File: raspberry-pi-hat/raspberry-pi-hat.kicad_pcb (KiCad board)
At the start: 2 copper layers, 6.6 x 9.1 mm, 28 parts, among them J1 IR_IN_JACK, J2 IR_OUT_JACK, J3 ADC0_JACK, J4 ADC1_JACK, J5 IR_IN_JMP, J6 IR_OUT_JMP, P1 RPi-GPIO, Q1 IRLML2803TRPBF, U1 MCP3204, U2 74AC86

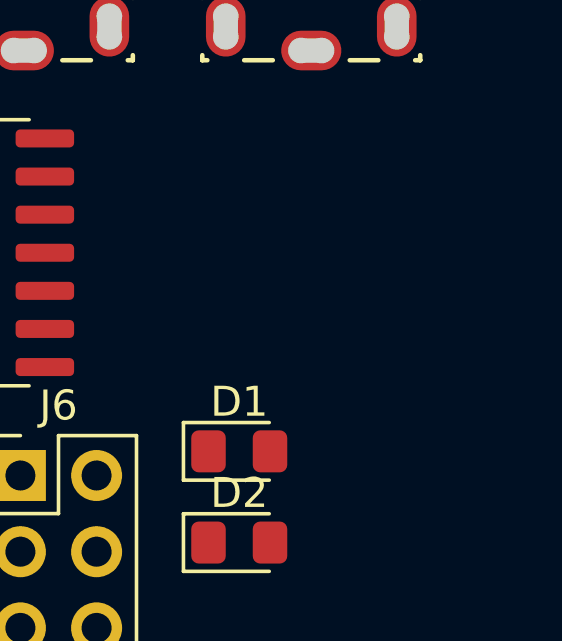
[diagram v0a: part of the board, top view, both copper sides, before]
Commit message: add initial state resistors
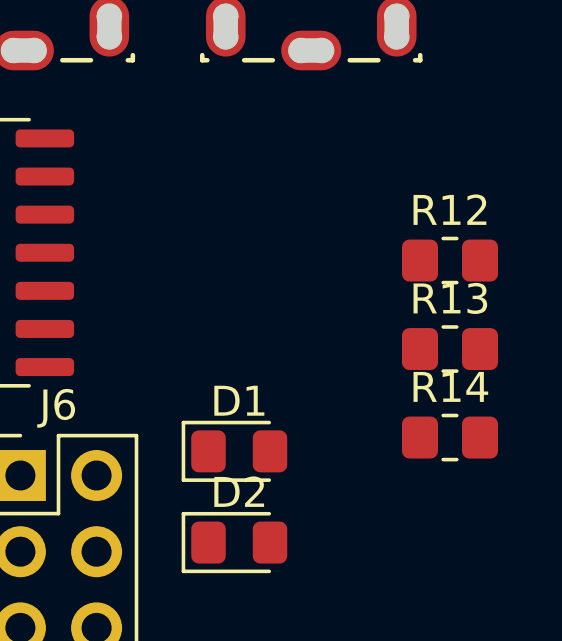
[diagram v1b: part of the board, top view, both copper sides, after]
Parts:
- added R12: 100K, Resistor_SMD:R_0805_2012Metric_Pad1.20x1.40mm_HandSolder, F.Cu at (94.0, 75.1)
- added R13: 100K, Resistor_SMD:R_0805_2012Metric_Pad1.20x1.40mm_HandSolder, F.Cu at (94.0, 78.0)
- added R14: 100K, Resistor_SMD:R_0805_2012Metric_Pad1.20x1.40mm_HandSolder, F.Cu at (94.0, 81.0)

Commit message: initial pcb
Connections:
- P1 pad 14: <NO NET> -> GND
- P1 pad 20: <NO NET> -> GND
- P1 pad 30: <NO NET> -> GND
- P1 pad 34: <NO NET> -> GND
- P1 pad 6: <NO NET> -> GND
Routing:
- added copper zone on B.Cu, net GND
- added copper zone on F.Cu, net GND
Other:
- board size 6.6 x 9.1 mm -> 58.5 x 66.5 mm

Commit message: pcb layout
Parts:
- removed C4: 0.1uF, Capacitor_SMD:C_0805_2012Metric_Pad1.18x1.45mm_HandSolder
- added C6: 100uF, Capacitor_SMD:CP_Elec_5x5.3, F.Cu at (53.5, 86.5)
- added C7: 100uF, Capacitor_SMD:CP_Elec_5x5.3, F.Cu at (64.0, 86.5)
- moved P1 42.2 mm to (93.0, 58.9)
- moved R2 36.0 mm to (81.5, 101.5), turned to 180 degrees
- moved R1 32.7 mm to (81.5, 94.0)
- moved R5 28.4 mm to (81.5, 99.0), turned to 180 degrees
- moved J3 26.4 mm to (53.5, 59.4)
- moved J4 25.7 mm to (63.8, 59.2)
- moved R3 25.2 mm to (81.5, 86.5)
- moved U1 25.1 mm to (56.0, 96.0), turned to -90 degrees
- moved J1 24.0 mm to (84.5, 59.2)
- moved R12 20.6 mm to (81.5, 91.5), turned to 180 degrees
- moved R14 19.9 mm to (81.5, 96.5), turned to 180 degrees
- moved U2 18.7 mm to (73.5, 93.0), turned to 180 degrees
- moved J5 17.1 mm to (87.0, 73.2), turned to -90 degrees
- moved R13 16.6 mm to (81.5, 89.0), turned to 180 degrees
- moved R4 16.5 mm to (73.5, 86.2), turned to 180 degrees
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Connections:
- C1 pad 2: <NO NET> -> GND
- C2 pad 2: <NO NET> -> GND
- C3 pad 2: <NO NET> -> GND
- C5 pad 2: <NO NET> -> GND
- D1 pad 1: <NO NET> -> GND
- J1 pad R2: Net-(J5-Pin_1) -> Net-(J5-Pin_5)
- J1 pad S: Net-(J5-Pin_1) -> Net-(J5-Pin_5)
- J1 pad T: Net-(J5-Pin_5) -> Net-(J5-Pin_1)
- J5 pad 6: <NO NET> -> GND
- J6 pad 3: Net-(D2-K) -> unconnected-(J6-Pin_3-Pad3)
- P1 pad 25: <NO NET> -> GND
- P1 pad 39: <NO NET> -> GND
- P1 pad 9: <NO NET> -> GND
- Q1 pad 2: <NO NET> -> GND
- R11 pad 1: <NO NET> -> GND
- R12 pad 1: <NO NET> -> GND
- R13 pad 1: <NO NET> -> GND
- R14 pad 1: <NO NET> -> GND
- R6 pad 1: <NO NET> -> GND
- U1 pad 12: <NO NET> -> GND
- U1 pad 3: <NO NET> -> GND
- U1 pad 4: <NO NET> -> GND
- U1 pad 7: <NO NET> -> GND
- U2 pad 10: <NO NET> -> GND
- U2 pad 12: <NO NET> -> GND
- U2 pad 13: <NO NET> -> GND
- U2 pad 7: <NO NET> -> GND
- U2 pad 9: <NO NET> -> GND
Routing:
- net +3.3V: track 0.00 -> 121.6 mm, vias 0 -> 4
- net /MOSI: track 0.00 -> 64.6 mm
- net /MISO: track 0.00 -> 63.7 mm, vias 0 -> 1
- net /ADC_CS: track 0.00 -> 63.6 mm
- net /SCLK: track 0.00 -> 57.8 mm, vias 0 -> 1
- net /ADC_CH1: track 0.00 -> 54.5 mm, vias 0 -> 4
- net /ADC_CH0: track 0.00 -> 49.2 mm
- net Net-(J5-Pin_4): track 0.00 -> 40.4 mm
- net /IR_OUT: track 0.00 -> 37.9 mm
- net /IR_IN: track 0.00 -> 34.3 mm
- net Net-(D2-K): track 0.00 -> 33.9 mm, vias 0 -> 3
- net /IR_IN_POL: track 0.00 -> 30.4 mm, vias 0 -> 1
- net /IR_OUT_POL: track 0.00 -> 30.2 mm, vias 0 -> 1
- net GND: track 0.00 -> 25.7 mm, vias 0 -> 30
- net Net-(J5-Pin_1): track 0.00 -> 25.1 mm
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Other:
- board size 58.5 x 66.5 mm -> 50.8 x 59 mm
- board text added: "IR Raspberry Pi Hat 2024-05-22"
